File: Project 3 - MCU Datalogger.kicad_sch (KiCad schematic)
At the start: 25 parts, among them U1 24LC1025, U2 24LC1025, U3 ATMEGA328P-AU, U4 DS1337S+, Y1 32.768 KHz, Y2 16 MHz

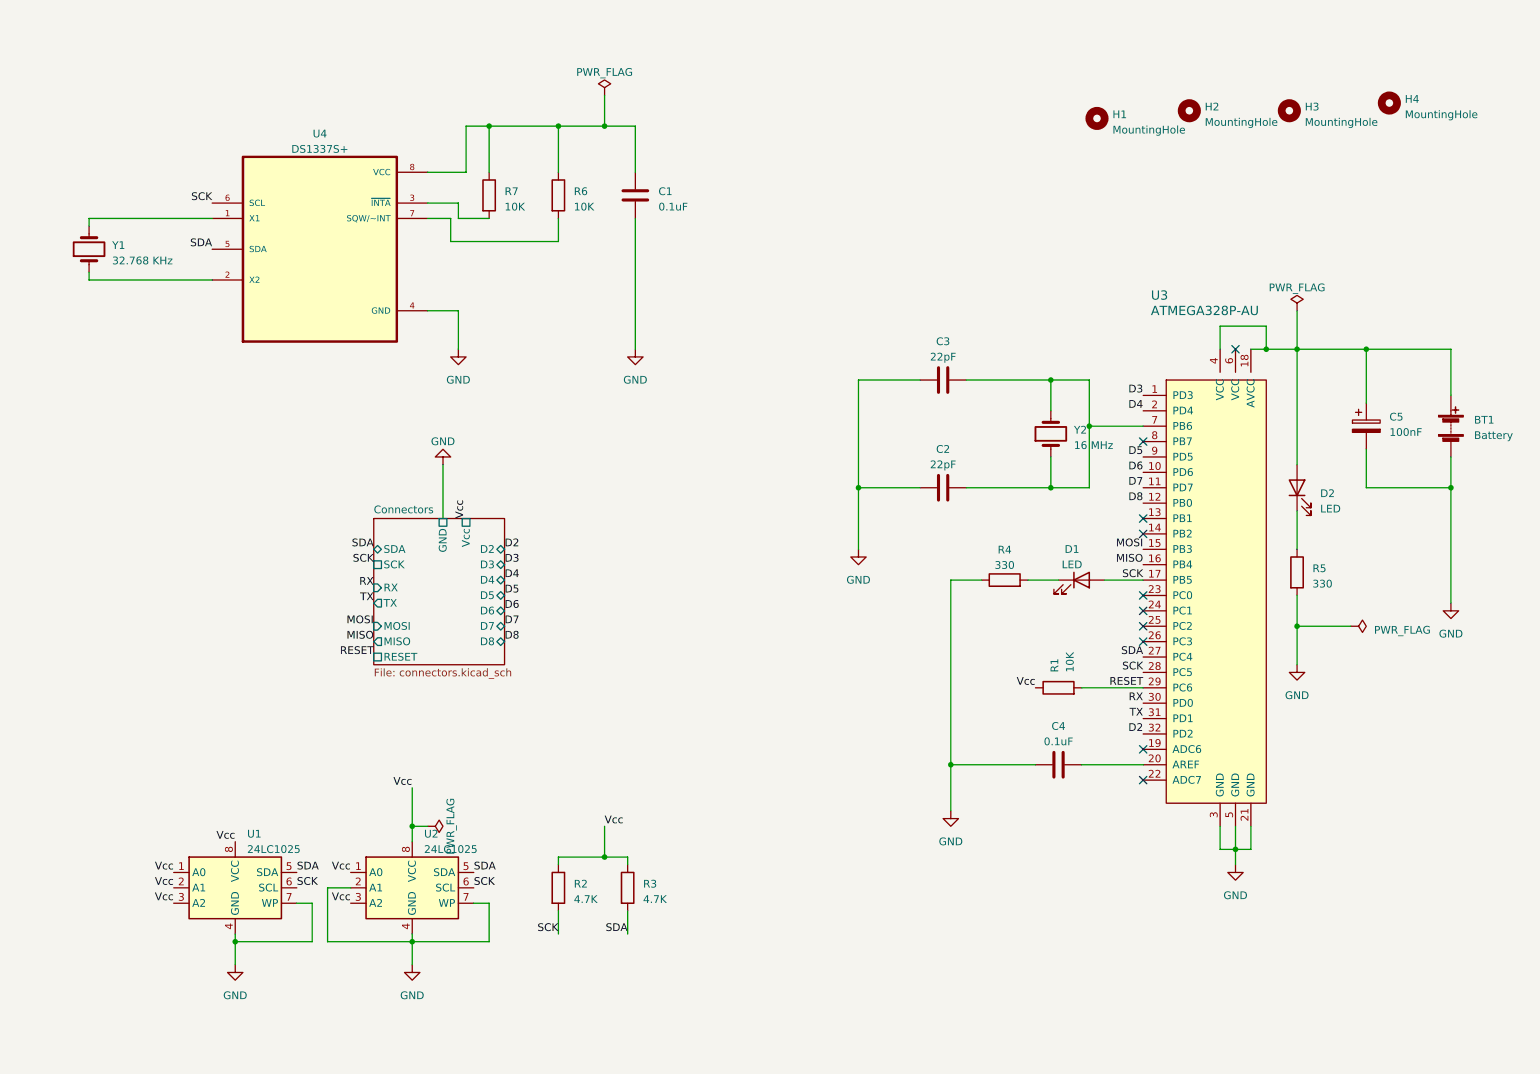
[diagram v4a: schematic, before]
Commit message: assigned power nets and added comments
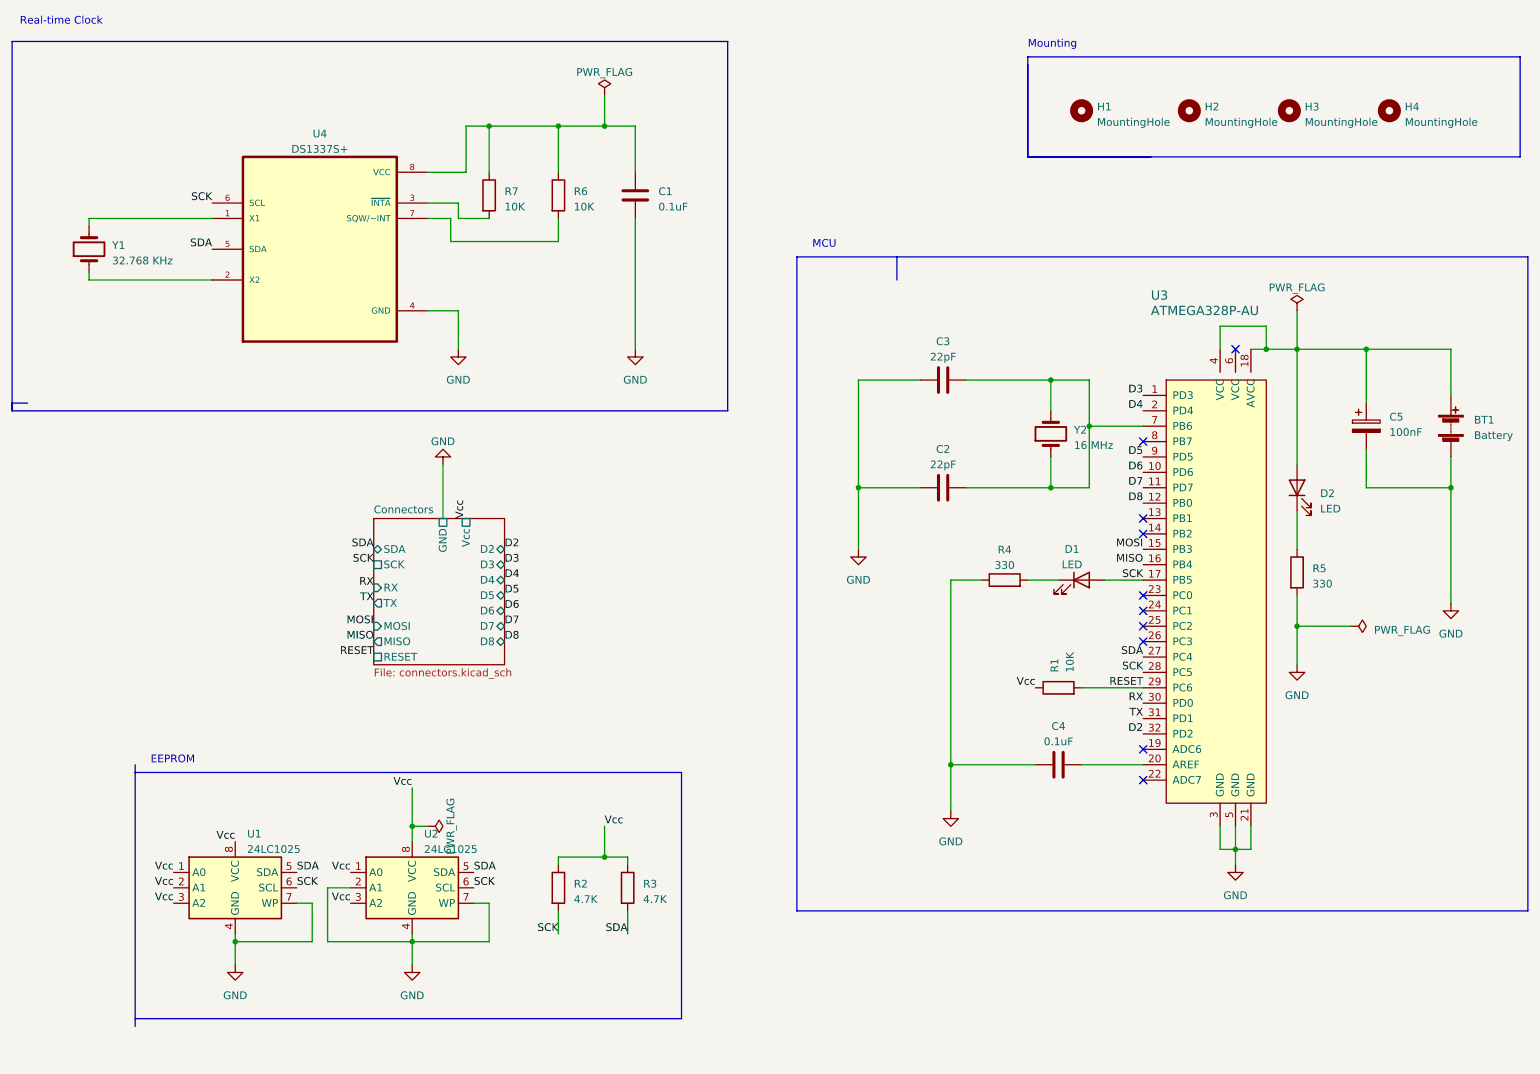
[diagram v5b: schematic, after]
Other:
- note added: "EEPROM"
- note added: "MCU"
- note added: "Mounting"
- note added: "Real-time Clock"
- moved on the sheet: H1, H4
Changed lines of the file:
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@@
   (no_connect (at 219.71 100.33))
   (no_connect (at 219.71 87.63))
+  (polyline (pts (xy 162.56 165.1) (xy 283.21 165.1))
+    (stroke (width 0) (type default))
+  )
   (wire (pts (xy 130.81 151.13) (xy 130.81 156.21))
     (stroke (width 0) (type default))
@@
     (stroke (width 0) (type default))
   )
+  (polyline (pts (xy 162.56 57.15) (xy 283.21 57.15))
+    (stroke (width 0) (type default))
+  )
   (wire (pts (xy 256.54 81.28) (xy 256.54 72.39))
     (stroke (width 0) (type default))
@@
     (stroke (width 0) (type default))
   )
+  (polyline (pts (xy 151.13 21.59) (xy 151.13 82.55))
+    (stroke (width 0) (type default))
+  )
   (wire (pts (xy 106.68 50.8) (xy 111.76 50.8))
     (stroke (width 0) (type default))
@@
     (stroke (width 0) (type default))
   )
+  (polyline (pts (xy 200.66 24.13) (xy 200.66 40.64))
+    (stroke (width 0) (type default))
+  )
   (wire (pts (xy 135.89 35.56) (xy 135.89 43.18))
     (stroke (width 0) (type default))
@@
     (stroke (width 0) (type default))
   )
+  (polyline (pts (xy 34.29 21.59) (xy 151.13 21.59))
+    (stroke (width 0) (type default))
+  )
   (wire (pts (xy 130.81 156.21) (xy 123.19 156.21))
     (stroke (width 0) (type default))
@@
     (stroke (width 0) (type default))
   )
+  (polyline (pts (xy 179.07 57.15) (xy 179.07 60.96))
+    (stroke (width 0) (type default))
+  )
   (wire (pts (xy 256.54 95.25) (xy 270.51 95.25))
     (stroke (width 0) (type default))
@@
     (stroke (width 0) (type default))
   )
+  (polyline (pts (xy 33.02 21.59) (xy 34.29 21.59))
+    (stroke (width 0) (type default))
+  )
   (wire (pts (xy 234.95 151.13) (xy 234.95 154.94))
     (stroke (width 0) (type default))
@@
     (stroke (width 0) (type default))
   )
+  (polyline (pts (xy 281.94 40.64) (xy 281.94 24.13))
+    (stroke (width 0) (type default))
+  )
   (wire (pts (xy 123.19 35.56) (xy 123.19 43.18))
     (stroke (width 0) (type default))
@@
     (stroke (width 0) (type default))
   )
+  (polyline (pts (xy 200.66 40.64) (xy 281.94 40.64))
+    (stroke (width 0) (type default))
+  )
   (wire (pts (xy 99.06 151.13) (xy 99.06 153.67))
     (stroke (width 0) (type default))
   )
+  (polyline (pts (xy 53.34 142.24) (xy 53.34 184.15))
+    (stroke (width 0) (type default))
+  )
+  (polyline (pts (xy 143.51 182.88) (xy 143.51 142.24))
+    (stroke (width 0) (type default))
+  )
   (wire (pts (xy 245.11 99.06) (xy 245.11 105.41))
     (stroke (width 0) (type default))
@@
     (stroke (width 0) (type default))
   )
+  (polyline (pts (xy 283.21 165.1) (xy 283.21 57.15))
+    (stroke (width 0) (type default))
+  )
+  (polyline (pts (xy 53.34 140.97) (xy 53.34 142.24))
+    (stroke (width 0) (type default))
+  )
+  (polyline (pts (xy 162.56 57.15) (xy 162.56 165.1))
+    (stroke (width 0) (type default))
+  )
+  (polyline (pts (xy 33.02 82.55) (xy 33.02 81.28))
+    (stroke (width 0) (type default))
+  )
   (wire (pts (xy 256.54 72.39) (xy 245.11 72.39))
     (stroke (width 0) (type default))
@@
     (stroke (width 0) (type default))
   )
+  (polyline (pts (xy 200.66 40.64) (xy 220.98 40.64))
+    (stroke (width 0) (type default))
+  )
   (wire (pts (xy 232.41 72.39) (xy 232.41 68.58))
     (stroke (width 0) (type default))
@@
     (stroke (width 0) (type default))
   )
+  (polyline (pts (xy 33.02 82.55) (xy 33.02 21.59))
+    (stroke (width 0) (type default))
+  )
+  (polyline (pts (xy 53.34 142.24) (xy 143.51 142.24))
+    (stroke (width 0) (type default))
+  )
   (wire (pts (xy 204.47 77.47) (xy 210.82 77.47))
     (stroke (width 0) (type default))
@@
     (stroke (width 0) (type default))
   )
+  (polyline (pts (xy 151.13 82.55) (xy 33.02 82.55))
+    (stroke (width 0) (type default))
+  )
   (wire (pts (xy 134.62 165.1) (xy 134.62 168.91))
     (stroke (width 0) (type default))
@@
     (stroke (width 0) (type default))
   )
+  (polyline (pts (xy 200.66 25.4) (xy 200.66 40.64))
+    (stroke (width 0) (type default))
+  )
+  (polyline (pts (xy 281.94 24.13) (xy 200.66 24.13))
+    (stroke (width 0) (type default))
+  )
   (wire (pts (xy 101.6 66.04) (xy 106.68 66.04))
     (stroke (width 0) (type default))
   )
+  (polyline (pts (xy 53.34 182.88) (xy 143.51 182.88))
+    (stroke (width 0) (type default))
+  )
   (wire (pts (xy 45.72 50.8) (xy 45.72 52.07))
     (stroke (width 0) (type default))
@@
   (wire (pts (xy 107.95 35.56) (xy 111.76 35.56))
     (stroke (width 0) (type default))
+  )
+  (polyline (pts (xy 33.02 81.28) (xy 35.56 81.28))
+    (stroke (width 0) (type default))
+  )
+  (text "Mounting" (at 200.66 22.86 0)
+    (effects (font (size 1.27 1.27)) (justify left bottom))
+  )
+  (text "Real-time Clock" (at 34.29 19.05 0)
+    (effects (font (size 1.27 1.27)) (justify left bottom))
+  )
+  (text "MCU" (at 165.1 55.88 0)
+    (effects (font (size 1.27 1.27)) (justify left bottom))
+  )
+  (text "EEPROM\n" (at 55.88 140.97 0)
+    (effects (font (size 1.27 1.27)) (justify left bottom))
   )
   (label "Vcc" (at 201.93 128.27 180) (fields_autoplaced)
@@
     )
   )
-  (symbol (lib_id "Mechanical:MountingHole") (at 260.35 31.75 0) (unit 1)
-    (in_bom yes) (on_board yes) (dnp no) (fields_autoplaced)
-    (property "Reference" "H4" (at 262.89 31.115 0)
-      (effects (font (size 1.27 1.27)) (justify left))
-    )
-    (property "Value" "MountingHole" (at 262.89 33.655 0)
-      (effects (font (size 1.27 1.27)) (justify left))
-    )
-    (property "Footprint" "MountingHole:MountingHole_2.1mm" (at 260.35 31.75 0)
-      (effects (font (size 1.27 1.27)) hide)
-    )
-    (property "Datasheet" "~" (at 260.35 31.75 0)
+  (symbol (lib_id "Mechanical:MountingHole") (at 260.35 33.02 0) (unit 1)
+    (in_bom yes) (on_board yes) (dnp no) (fields_autoplaced)
+    (property "Reference" "H4" (at 262.89 32.385 0)
+      (effects (font (size 1.27 1.27)) (justify left))
+    )
+    (property "Value" "MountingHole" (at 262.89 34.925 0)
+      (effects (font (size 1.27 1.27)) (justify left))
+    )
+    (property "Footprint" "MountingHole:MountingHole_2.1mm" (at 260.35 33.02 0)
+      (effects (font (size 1.27 1.27)) hide)
+    )
+    (property "Datasheet" "~" (at 260.35 33.02 0)
       (effects (font (size 1.27 1.27)) hide)
     )
@@
     )
   )
-  (symbol (lib_id "Mechanical:MountingHole") (at 212.09 34.29 0) (unit 1)
-    (in_bom yes) (on_board yes) (dnp no) (fields_autoplaced)
-    (property "Reference" "H1" (at 214.63 33.655 0)
-      (effects (font (size 1.27 1.27)) (justify left))
-    )
-    (property "Value" "MountingHole" (at 214.63 36.195 0)
-      (effects (font (size 1.27 1.27)) (justify left))
-    )
-    (property "Footprint" "MountingHole:MountingHole_2.1mm" (at 212.09 34.29 0)
-      (effects (font (size 1.27 1.27)) hide)
-    )
-    (property "Datasheet" "~" (at 212.09 34.29 0)
-      (effects (font (size 1.27 1.27)) hide)
-    )
+  (symbol (lib_id "Mechanical:MountingHole") (at 209.55 33.02 0) (unit 1)
+    (in_bom yes) (on_board yes) (dnp no) (fields_autoplaced)
+    (property "Reference" "H1" (at 212.09 32.385 0)
+      (effects (font (size 1.27 1.27)) (justify left))
+    )
+    (property "Value" "MountingHole" (at 212.09 34.925 0)
+      (effects (font (size 1.27 1.27)) (justify left))
+    )
+    (property "Footprint" "MountingHole:MountingHole_2.1mm" (at 209.55 33.02 0)
+      (effects (font (size 1.27 1.27)) hide)
+    )
+    (property "Datasheet" "~" (at 209.55 33.02 0)
+      (effects (font (size 1.27 1.27)) hide)
+    )

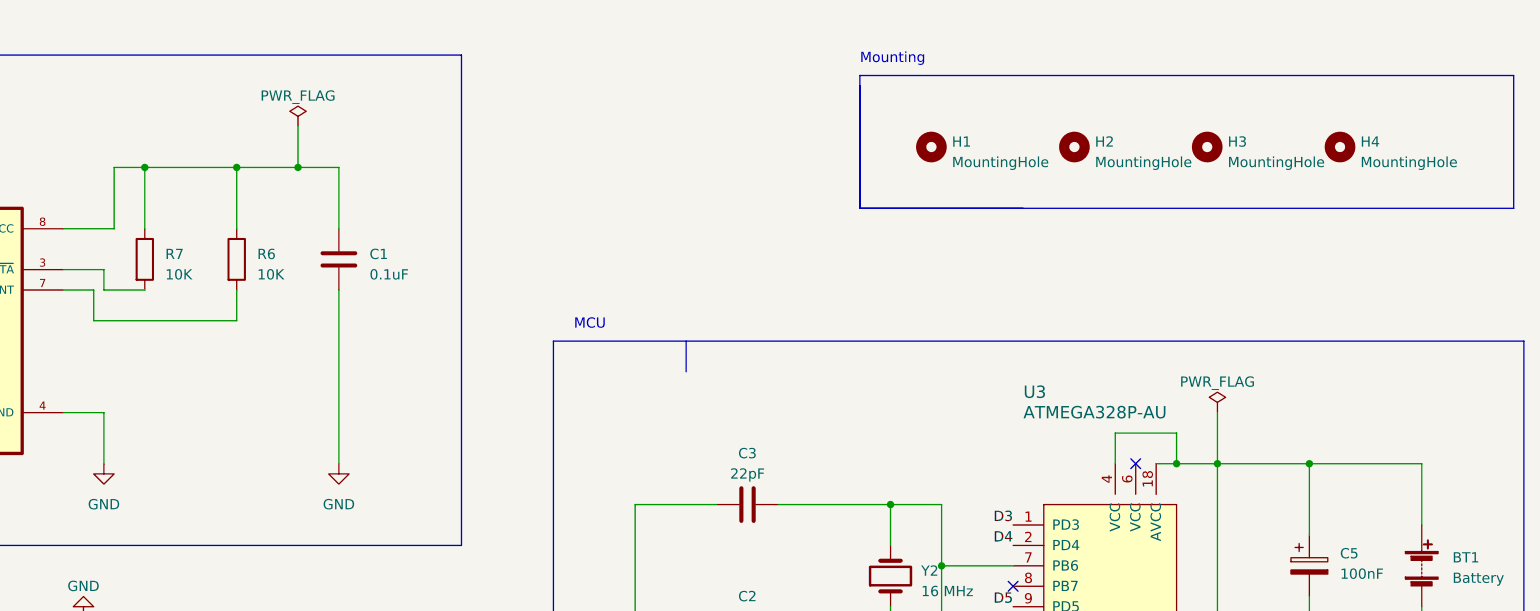
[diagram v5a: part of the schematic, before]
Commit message: fixed wiring violations and added silkscreen labels
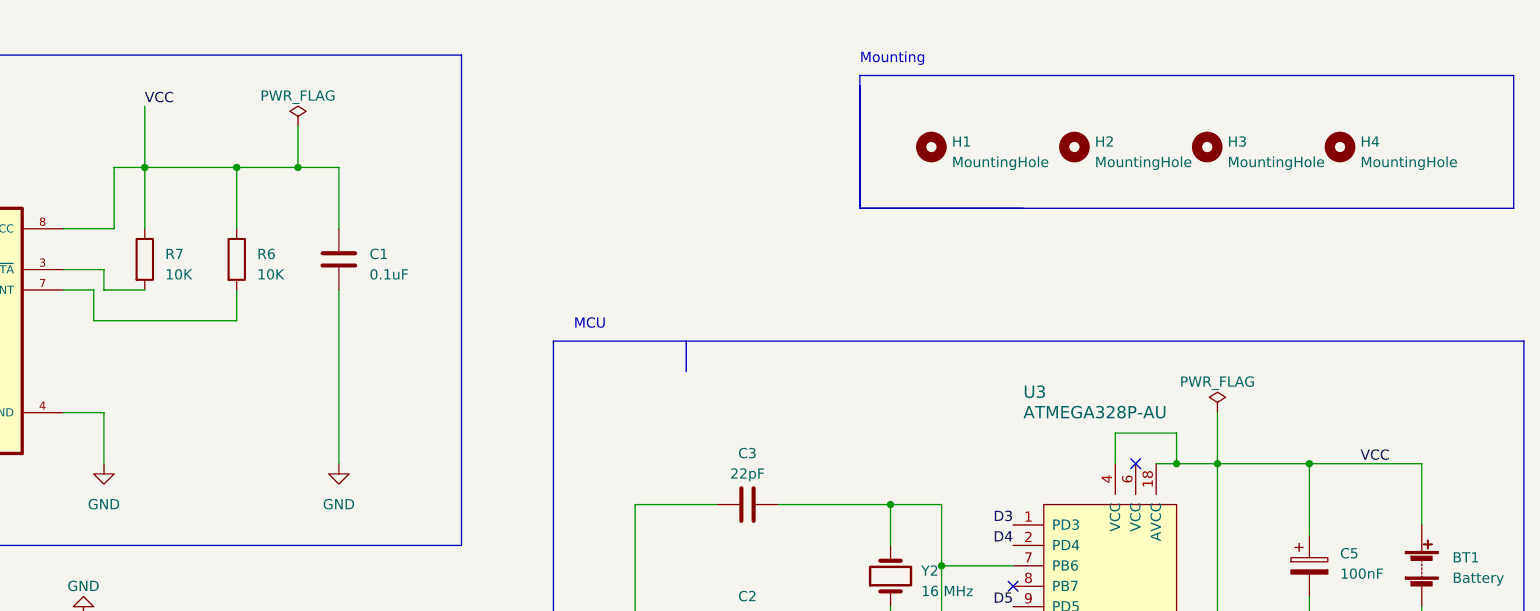
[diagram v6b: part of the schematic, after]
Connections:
- net VCC: now reaches BT1.1 (+), C5.1, D2.2 (A), U3.18 (AVCC), U3.4 (VCC)
- net VCC: now also C1.1, R6.1, R7.1, U4.8 (VCC)
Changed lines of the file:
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@@
+    (stroke (width 0) (type default))
+  )
+  (wire (pts (xy 111.76 27.94) (xy 111.76 35.56))
     (stroke (width 0) (type default))
   )
@@
     (effects (font (size 1.27 1.27)) (justify right bottom))
   )
+  (label "VCC" (at 111.76 27.94 0) (fields_autoplaced)
+    (effects (font (size 1.27 1.27)) (justify left bottom))
+  )
   (label "D8" (at 114.3 120.65 0) (fields_autoplaced)
     (effects (font (size 1.27 1.27)) (justify left bottom))
@@
     (effects (font (size 1.27 1.27)) (justify right bottom))
   )
+  (label "VCC" (at 262.89 72.39 0) (fields_autoplaced)
+    (effects (font (size 1.27 1.27)) (justify left bottom))
+  )
   (label "TX" (at 219.71 133.35 180) (fields_autoplaced)
